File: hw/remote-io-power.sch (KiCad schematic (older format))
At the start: 9 parts, among them Q1 DMG2305UX, Q2 DMMT5401, U1 AP1506

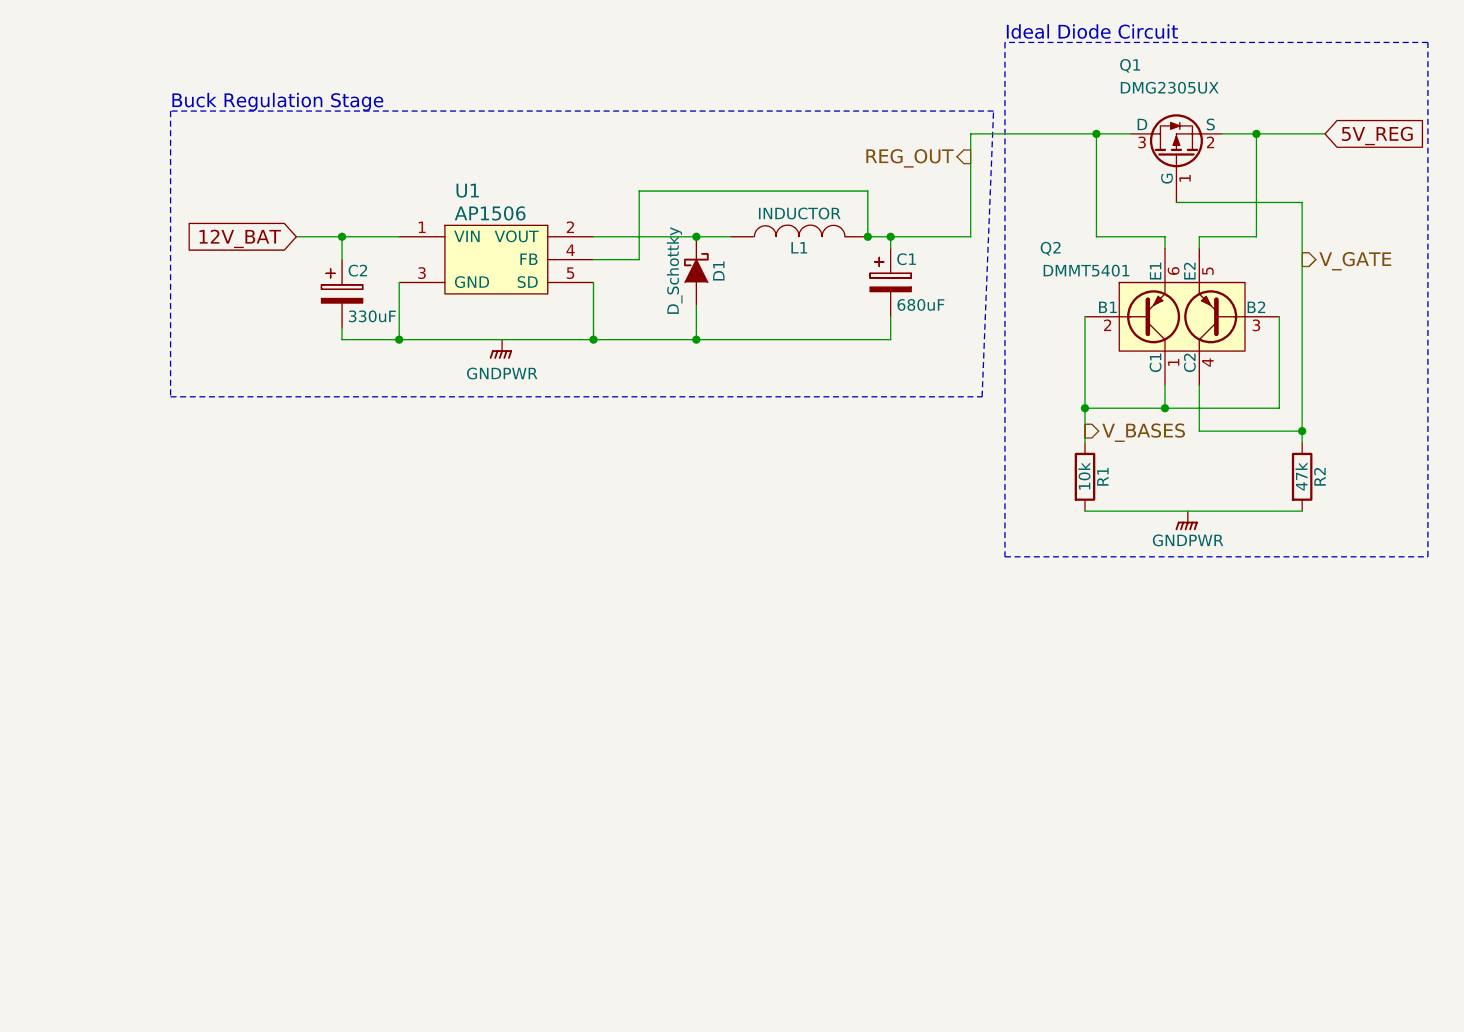
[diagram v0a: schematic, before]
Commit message: Added ADC schematic and connections
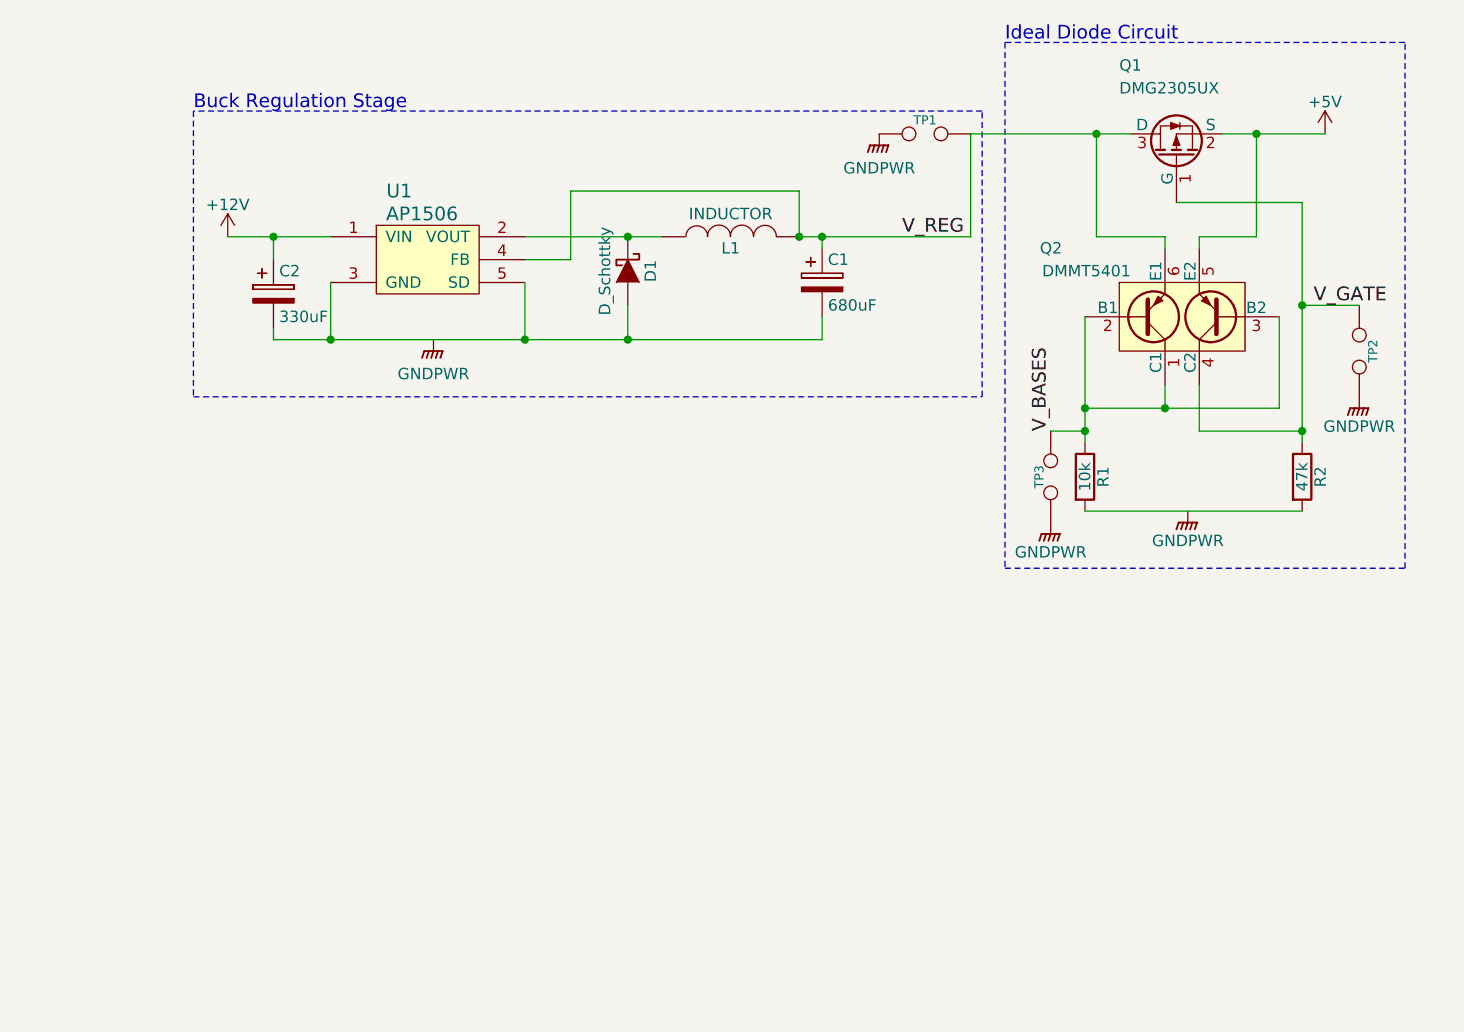
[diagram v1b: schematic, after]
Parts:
- added TP1, TP2, TP3: TEST, symbol TEST
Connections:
- net GNDPWR: now also TP1.1, TP2.2, TP3.2
- net V_BASES: now also TP3.1
- net V_GATE: now also TP2.1
- net at U1.3 (TAB): now also C1.2, C2.2, D1.2 (A), U1.5 (SD)
- net 12V_BAT renamed +12V
- net 5V_REG renamed +5V
- net REG_OUT renamed V_REG
- net V_REG: now also TP1.2
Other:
- moved on the sheet: C1, C2, D1, L1, U1

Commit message: Added I2C ID EEPROM
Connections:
- net at U1.3 (TAB): now also C1.2, C2.2, D1.2 (A), U1.5 (SD)
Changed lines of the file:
@@
 $Descr USLetter 11000 8500
 encoding utf-8
-Sheet 2 3
+Sheet 2 4
 Title "Remote I/O Power Section"
 Date "2015-06-15"

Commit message: Added RS-422 Receiver Circuit
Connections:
- net at U1.3 (TAB): now also C1.2, C2.2, D1.2 (A), U1.5 (SD)
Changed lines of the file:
@@
 $Descr USLetter 11000 8500
 encoding utf-8
-Sheet 2 4
+Sheet 2 5
 Title "Remote I/O Power Section"
 Date "2015-06-15"

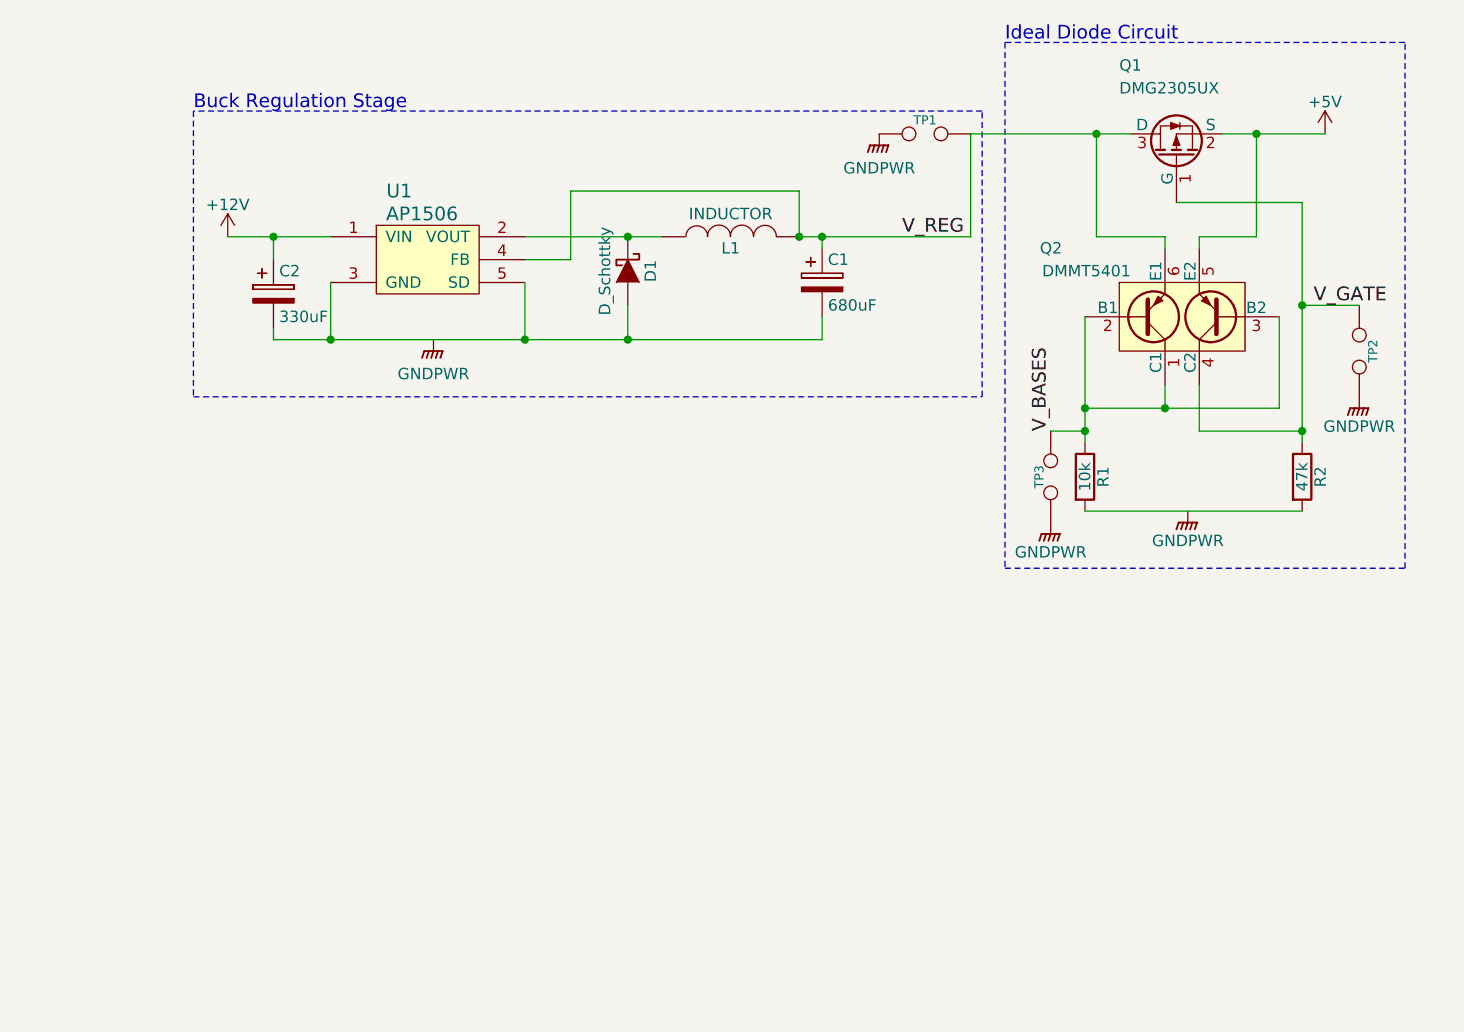
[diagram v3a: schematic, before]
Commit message: Matched all footprints to schem and created kicad_pcb file
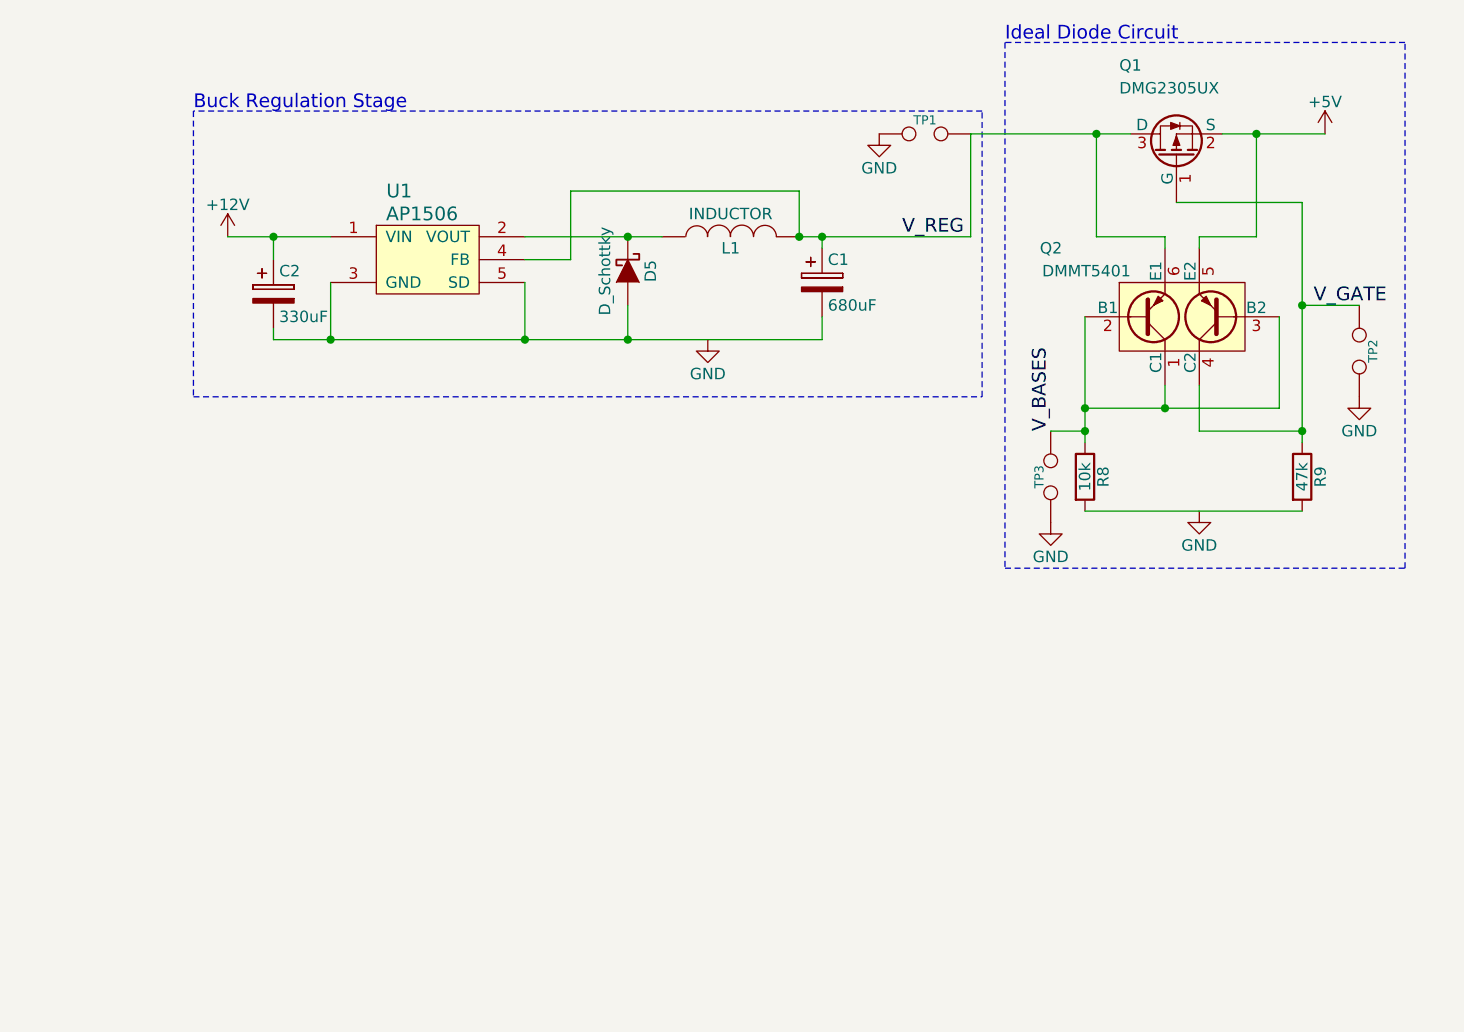
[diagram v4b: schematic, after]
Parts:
- C1: footprint (none) -> Capacitors_ThroughHole:C_Radial_D12.5_L25_P5
- C2: footprint (none) -> Capacitors_ThroughHole:C_Radial_D10_L25_P5
- D5: renamed from D1; footprint (none) -> Diodes_SMD:Diode-SMB_Handsoldering
- L1: footprint (none) -> remote-io:SRN1060-XXXM
- Q1: footprint (none) -> Housings_SOT-23_SOT-143_TSOT-6:SOT-23_Handsoldering
- Q2: footprint (none) -> Housings_SOT-23_SOT-143_TSOT-6:SOT-23-6
- R8: renamed from R1; footprint (none) -> Resistors_SMD:R_0805_HandSoldering
- R9: renamed from R2; footprint (none) -> Resistors_SMD:R_0805_HandSoldering
- TP1, TP2, TP3: footprint (none) -> Connect:TESTPOINT
- U1: footprint (none) -> SMD_Packages:TO-263-5_HandSoldering
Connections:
- net at U1.3 (TAB): now also C1.2, C2.2, D5.2 (A), U1.5 (SD)
- net GNDPWR renamed GND
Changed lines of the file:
@@
 U 1 1 557EE55F
 P 3800 3550
-AR Path="/557EE55F" Ref="U1"  Part="1"
-AR Path="/557F39A6/557EE55F" Ref="U1"  Part="1"
 F 0 "U1" H 3700 3850 60  0000 C CNN
 F 1 "AP1506" H 3800 3750 60  0000 C CNN
-F 2 "" H 4200 3500 60  0001 C CNN
+F 2 "SMD_Packages:TO-263-5_HandSoldering" H 4200 3500 60  0001 C CNN
 F 3 "" H 4200 3500 60  0000 C CNN
 	1    3800 3550
@@
 F 0 "C2" H 3175 3800 50  0000 L CNN
 F 1 "330uF" H 3175 3600 50  0000 L CNN
-F 2 "" H 3188 3550 30  0000 C CNN
+F 2 "Capacitors_ThroughHole:C_Radial_D10_L25_P5" H 3188 3550 30  0001 C CNN
 F 3 "" H 3150 3700 60  0000 C CNN
 	1    3150 3700
@@
 F 0 "C1" H 5575 3750 50  0000 L CNN
 F 1 "680uF" H 5575 3550 50  0000 L CNN
-F 2 "" H 5588 3500 30  0000 C CNN
+F 2 "Capacitors_ThroughHole:C_Radial_D12.5_L25_P5" H 5588 3500 30  0001 C CNN
 F 3 "" H 5550 3650 60  0000 C CNN
 	1    5550 3650
@@
 F 0 "L1" V 5100 3450 50  0000 C CNN
 F 1 "INDUCTOR" V 5250 3450 50  0000 C CNN
-F 2 "" H 5150 3450 60  0000 C CNN
+F 2 "remote-io:SRN1060-XXXM" H 5150 3450 60  0001 C CNN
 F 3 "" H 5150 3450 60  0000 C CNN
 	1    5150 3450
@@
 $EndComp
 $Comp
-L D_Schottky D1
+L D_Schottky D5
 U 1 1 557EE6C3
 P 4700 3600
-F 0 "D1" H 4700 3700 50  0000 C CNN
+F 0 "D5" H 4700 3700 50  0000 C CNN
 F 1 "D_Schottky" H 4700 3500 50  0000 C CNN
-F 2 "" H 4700 3600 60  0000 C CNN
+F 2 "Diodes_SMD:Diode-SMB_Handsoldering" H 4700 3600 60  0001 C CNN
 F 3 "" H 4700 3600 60  0000 C CNN
 	1    4700 3600
@@
 Wire Wire Line
 	2950 3450 3400 3450
-$Comp
-L GNDPWR #PWR17
-U 1 1 557EE725
-P 3850 3900
-F 0 "#PWR17" H 3850 3700 50  0001 C CNN
-F 1 "GNDPWR" H 3850 3750 50  0000 C CNN
-F 2 "" H 3850 3850 60  0000 C CNN
-F 3 "" H 3850 3850 60  0000 C CNN
-	1    3850 3900
-	1    0    0    -1
-$EndComp
 Wire Wire Line
 	3150 3850 3150 3900
@@
 F 0 "Q2" H 6600 4100 50  0000 R CNN
 F 1 "DMMT5401" H 6900 4000 50  0000 R CNN
-F 2 "" H 7150 3700 29  0000 C CNN
+F 2 "Housings_SOT-23_SOT-143_TSOT-6:SOT-23-6" H 7150 3700 29  0001 C CNN
 F 3 "" H 6950 3800 60  0000 C CNN
 	1    7100 3800
@@
 F 0 "Q1" V 7500 3350 50  0000 R CNN
 F 1 "DMG2305UX" V 7400 3350 50  0000 R CNN
-F 2 "" H 7300 3200 29  0000 C CNN
+F 2 "Housings_SOT-23_SOT-143_TSOT-6:SOT-23_Handsoldering" H 7300 3200 29  0001 C CNN
 F 3 "" H 7100 3100 60  0000 C CNN
 	1    7100 3100
@@
 Connection ~ 6700 4200
 $Comp
-L R R1
+L R R8
 U 1 1 557F07EA
 P 6700 4500
-F 0 "R1" V 6780 4500 50  0000 C CNN
+F 0 "R8" V 6780 4500 50  0000 C CNN
 F 1 "10k" V 6700 4500 50  0000 C CNN
-F 2 "" V 6630 4500 30  0000 C CNN
+F 2 "Resistors_SMD:R_0805_HandSoldering" V 6630 4500 30  0001 C CNN
 F 3 "" H 6700 4500 30  0000 C CNN
 	1    6700 4500
@@
 $EndComp
 $Comp
-L R R2
+L R R9
 U 1 1 557F08A4
 P 7650 4500
-F 0 "R2" V 7730 4500 50  0000 C CNN
+F 0 "R9" V 7730 4500 50  0000 C CNN
 F 1 "47k" V 7650 4500 50  0000 C CNN
-F 2 "" V 7580 4500 30  0000 C CNN
+F 2 "Resistors_SMD:R_0805_HandSoldering" V 7580 4500 30  0001 C CNN
 F 3 "" H 7650 4500 30  0000 C CNN
 	1    7650 4500
-	1    0    0    -1
-$EndComp
-$Comp
-L GNDPWR #PWR19
-U 1 1 557F312B
-P 7150 4650
-F 0 "#PWR19" H 7150 4450 50  0001 C CNN
-F 1 "GNDPWR" H 7150 4520 50  0000 C CNN
-F 2 "" H 7150 4600 60  0000 C CNN
-F 3 "" H 7150 4600 60  0000 C CNN
-	1    7150 4650
 	1    0    0    -1
 $EndComp
@@
 Ideal Diode Circuit
 $Comp
-L +12V #PWR16
+L +12V #PWR026
 U 1 1 557F7629
 P 2950 3450
-F 0 "#PWR16" H 2950 3300 50  0001 C CNN
+F 0 "#PWR026" H 2950 3300 50  0001 C CNN
 F 1 "+12V" H 2950 3590 50  0000 C CNN
 F 2 "" H 2950 3450 60  0000 C CNN
@@
 $EndComp
 $Comp
-L +5V #PWR15
+L +5V #PWR027
 U 1 1 557F764F
 P 7750 3000
-F 0 "#PWR15" H 7750 2850 50  0001 C CNN
+F 0 "#PWR027" H 7750 2850 50  0001 C CNN
 F 1 "+5V" H 7750 3140 50  0000 C CNN
 F 2 "" H 7750 3000 60  0000 C CNN
@@
 F 0 "TP1" H 6000 3060 40  0000 C CNN
 F 1 "TEST" H 6000 2930 40  0001 C CNN
-F 2 "" H 6000 3000 60  0000 C CNN
+F 2 "Connect:TESTPOINT" H 6000 3000 60  0001 C CNN
 F 3 "" H 6000 3000 60  0000 C CNN
 	1    6000 3000
-	1    0    0    -1
-$EndComp
-$Comp
-L GNDPWR #PWR14
-U 1 1 557F9C6D
-P 5800 3000
-F 0 "#PWR14" H 5800 2800 50  0001 C CNN
-F 1 "GNDPWR" H 5800 2850 50  0000 C CNN
-F 2 "" H 5800 2950 60  0000 C CNN
-F 3 "" H 5800 2950 60  0000 C CNN
-	1    5800 3000
 	1    0    0    -1
 $EndComp
@@
 F 0 "TP2" H 7900 4010 40  0000 C CNN
 F 1 "TEST" H 7900 3880 40  0001 C CNN
-F 2 "" H 7900 3950 60  0000 C CNN
+F 2 "Connect:TESTPOINT" H 7900 3950 60  0001 C CNN
 F 3 "" H 7900 3950 60  0000 C CNN
 	1    7900 3950
@@
 F 0 "TP3" H 6550 4450 40  0000 C CNN
 F 1 "TEST" H 6550 4430 40  0001 C CNN
-F 2 "" H 6550 4500 60  0000 C CNN
+F 2 "Connect:TESTPOINT" H 6550 4500 60  0001 C CNN
 F 3 "" H 6550 4500 60  0000 C CNN
 	1    6550 4500
@@
 Connection ~ 6700 4300
 Connection ~ 7650 3750
-$Comp
-L GNDPWR #PWR20
-U 1 1 557FA308
-P 6550 4700
-F 0 "#PWR20" H 6550 4500 50  0001 C CNN
-F 1 "GNDPWR" H 6550 4570 50  0000 C CNN
-F 2 "" H 6550 4650 60  0000 C CNN
-F 3 "" H 6550 4650 60  0000 C CNN
-	1    6550 4700
-	1    0    0    -1
-$EndComp
-$Comp
-L GNDPWR #PWR18
-U 1 1 557FA35B
-P 7900 4150
-F 0 "#PWR18" H 7900 3950 50  0001 C CNN
-F 1 "GNDPWR" H 7900 4020 50  0000 C CNN
-F 2 "" H 7900 4100 60  0000 C CNN
-F 3 "" H 7900 4100 60  0000 C CNN
-	1    7900 4150
-	1    0    0    -1
-$EndComp
 Wire Wire Line
 	6550 4300 6700 4300
@@
 Text Label 7700 3750 0    60   ~ 0
 V_GATE
+$Comp
+L GND #PWR028
+U 1 1 5582FAEC
+P 5050 3900
+F 0 "#PWR028" H 5050 3650 50  0001 C CNN
+F 1 "GND" H 5050 3750 50  0000 C CNN
+F 2 "" H 5050 3900 60  0000 C CNN
+F 3 "" H 5050 3900 60  0000 C CNN
+	1    5050 3900
+	1    0    0    -1
+$EndComp
+$Comp
+L GND #PWR029
+U 1 1 5582FB3E
+P 6550 4700
+F 0 "#PWR029" H 6550 4450 50  0001 C CNN
+F 1 "GND" H 6550 4550 50  0000 C CNN
+F 2 "" H 6550 4700 60  0000 C CNN
+F 3 "" H 6550 4700 60  0000 C CNN
+	1    6550 4700
+	1    0    0    -1
+$EndComp
+$Comp
+L GND #PWR030
+U 1 1 5582FB61
+P 7200 4650
+F 0 "#PWR030" H 7200 4400 50  0001 C CNN
+F 1 "GND" H 7200 4500 50  0000 C CNN
+F 2 "" H 7200 4650 60  0000 C CNN
+F 3 "" H 7200 4650 60  0000 C CNN
+	1    7200 4650
+	1    0    0    -1
+$EndComp
+$Comp
+L GND #PWR031
+U 1 1 5582FB89
+P 5800 3000
+F 0 "#PWR031" H 5800 2750 50  0001 C CNN
+F 1 "GND" H 5800 2850 50  0000 C CNN
+F 2 "" H 5800 3000 60  0000 C CNN
+F 3 "" H 5800 3000 60  0000 C CNN
+	1    5800 3000
+	1    0    0    -1
+$EndComp
+$Comp
+L GND #PWR032
+U 1 1 5582FBB1
+P 7900 4150
+F 0 "#PWR032" H 7900 3900 50  0001 C CNN
+F 1 "GND" H 7900 4000 50  0000 C CNN
+F 2 "" H 7900 4150 60  0000 C CNN
+F 3 "" H 7900 4150 60  0000 C CNN
+	1    7900 4150
+	1    0    0    -1
+$EndComp
 $EndSCHEMATC

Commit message: removed autosave
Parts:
- TP1, TP2, TP3: footprint Connect:TESTPOINT -> Pin_Headers:Pin_Header_Straight_1x02
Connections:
- net at U1.3 (TAB): now also C1.2, C2.2, D5.2 (A), U1.5 (SD)
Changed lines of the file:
@@
 F 0 "TP1" H 6000 3060 40  0000 C CNN
 F 1 "TEST" H 6000 2930 40  0001 C CNN
-F 2 "Connect:TESTPOINT" H 6000 3000 60  0001 C CNN
+F 2 "Pin_Headers:Pin_Header_Straight_1x02" H 6000 3000 60  0001 C CNN
 F 3 "" H 6000 3000 60  0000 C CNN
 	1    6000 3000
@@
 F 0 "TP2" H 7900 4010 40  0000 C CNN
 F 1 "TEST" H 7900 3880 40  0001 C CNN
-F 2 "Connect:TESTPOINT" H 7900 3950 60  0001 C CNN
+F 2 "Pin_Headers:Pin_Header_Straight_1x02" H 7900 3950 60  0001 C CNN
 F 3 "" H 7900 3950 60  0000 C CNN
 	1    7900 3950
@@
 F 0 "TP3" H 6550 4450 40  0000 C CNN
 F 1 "TEST" H 6550 4430 40  0001 C CNN
-F 2 "Connect:TESTPOINT" H 6550 4500 60  0001 C CNN
+F 2 "Pin_Headers:Pin_Header_Straight_1x02" H 6550 4500 60  0001 C CNN
 F 3 "" H 6550 4500 60  0000 C CNN
 	1    6550 4500
